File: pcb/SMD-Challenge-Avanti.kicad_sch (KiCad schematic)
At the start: 14 parts, among them SW1 SW_SPDT, U1 SN74LVC1G14DBV, U2 74HC4017

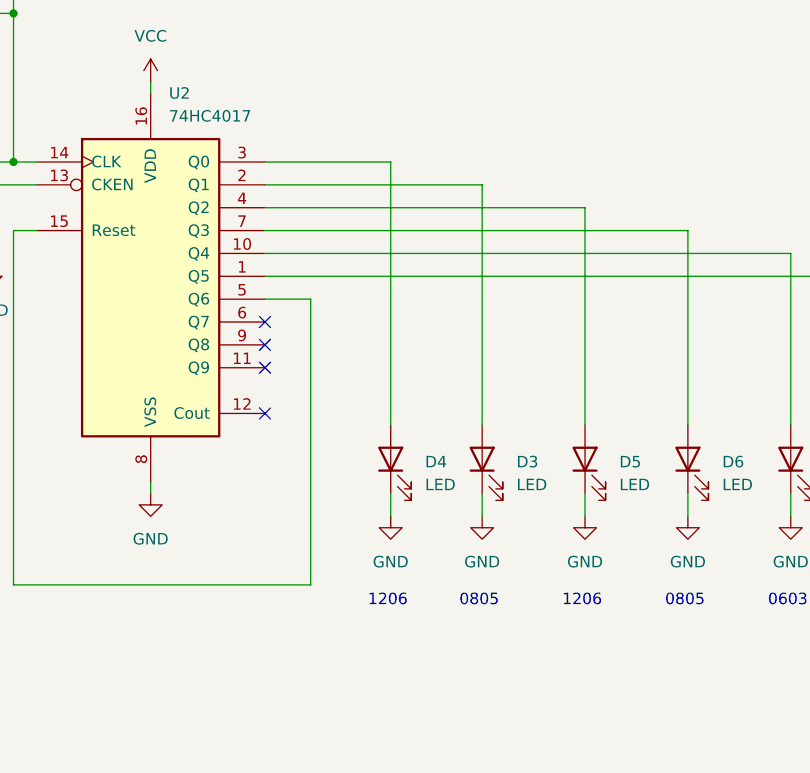
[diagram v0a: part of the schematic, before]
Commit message: Fix blink order
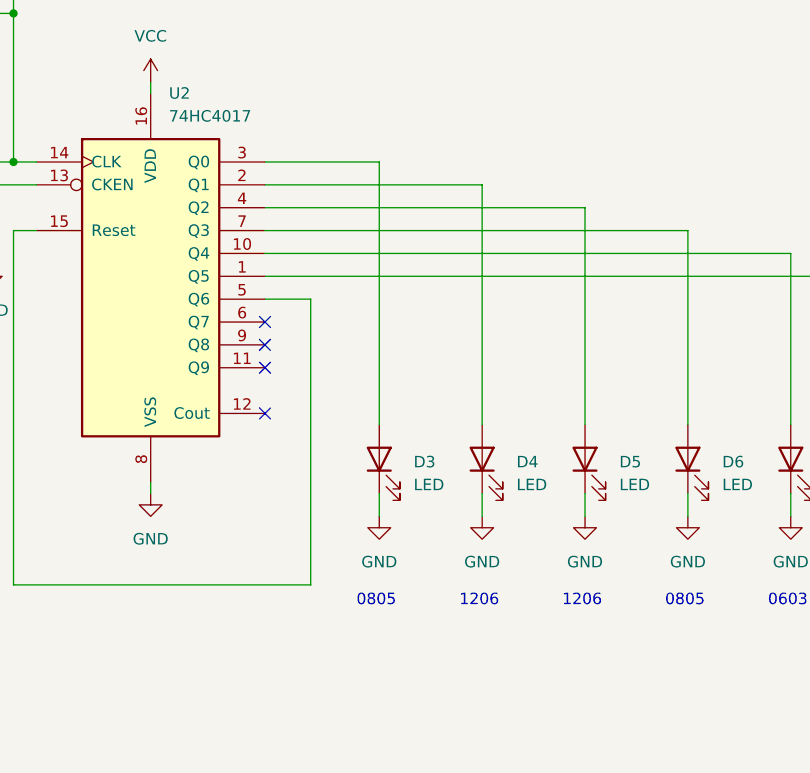
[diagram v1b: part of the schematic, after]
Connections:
- net at D4.2 (A): now also U2.2 (Q1); no longer U2.3 (Q0)
- net at D3.2 (A): now also U2.3 (Q0); no longer U2.2 (Q1)
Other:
- moved on the sheet: D3, D4
